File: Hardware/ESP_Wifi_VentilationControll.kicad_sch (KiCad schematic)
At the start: 38 parts, among them J1 programming, Q1 2N3904, Q2 2N3904, SW1 RST, SW2 BOOT, U1 LM1117-3.3, U2 ESP-12E, U3 ILD207T_D207, U4 ILD207T_D207, U5 XD-45_MH_MINI

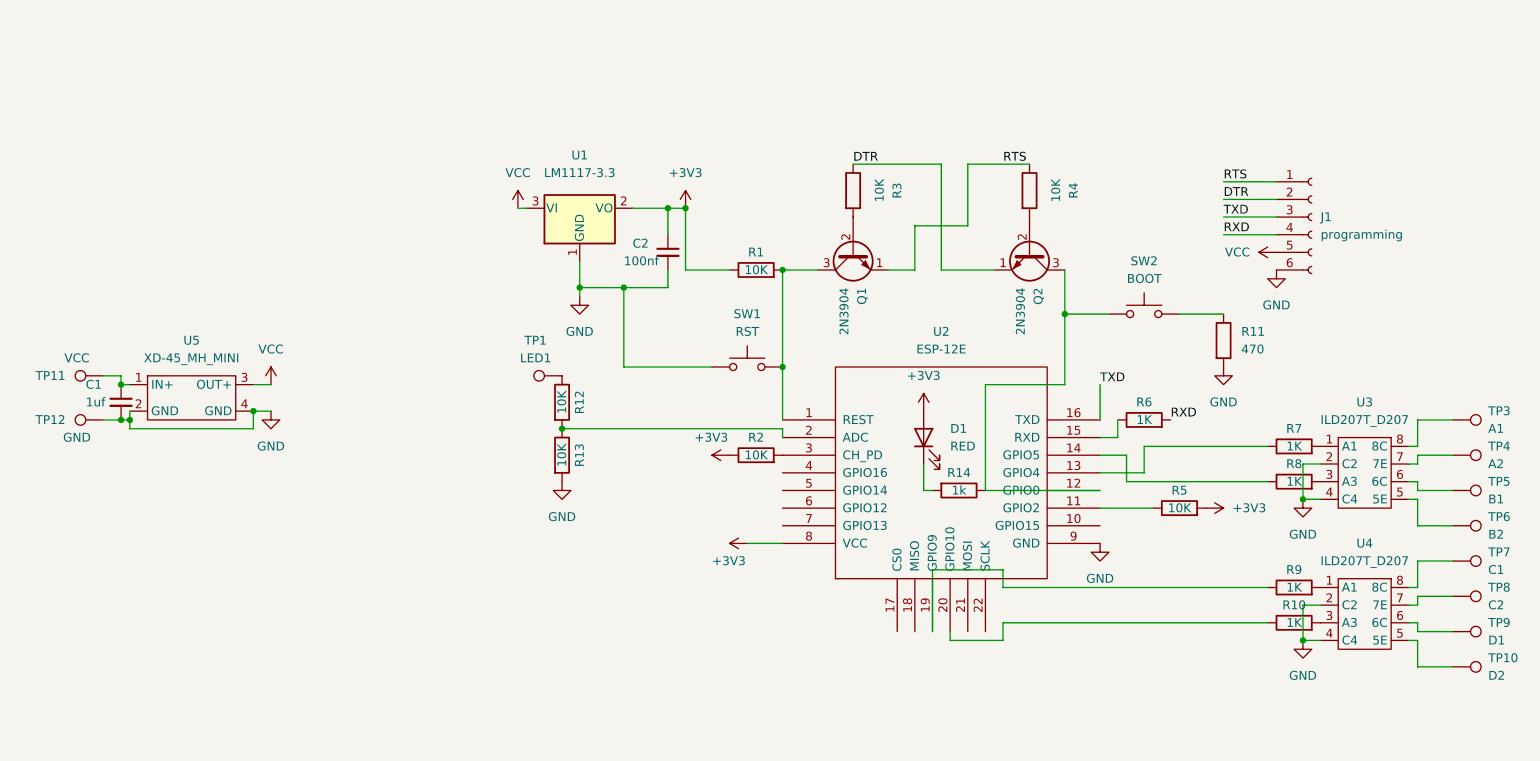
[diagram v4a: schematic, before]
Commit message: fixed some footprints and added missing resistor
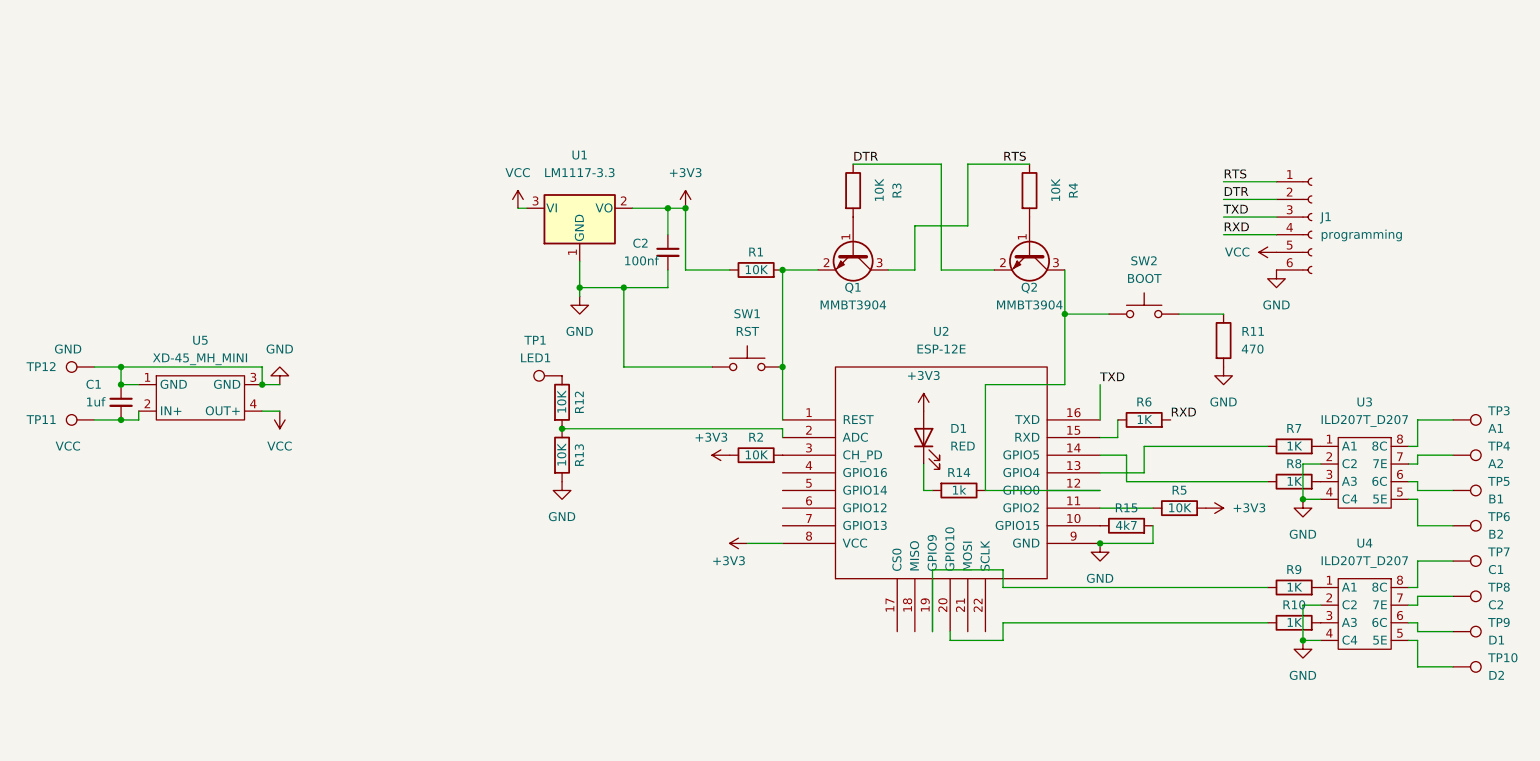
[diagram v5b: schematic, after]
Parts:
- removed Q1, Q2: 2N3904, Package_TO_SOT_SMD:SOT-23, symbol Transistor_BJT:2N3904
- added Q1, Q2: MMBT3904, Package_TO_SOT_SMD:SOT-23, symbol Transistor_BJT:MMBT3904
- added R15: 4k7, Resistor_SMD:R_1206_3216Metric, symbol Device:R
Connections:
- net DTR: now also Q2.2 (E)
- net GND: now also C1.1, U5.1 (GND), U5.3 (GND), R15.2; no longer C1.2, U5.2 (GND), U5.4 (GND)
- net RTS: now also Q1.3 (C)
- net VCC: now also U5.4 (OUT+); no longer U5.3 (OUT+)
- net at R1.2, SW1.2, U2.1 (REST): now also Q1.2 (E)
- net at U2.10 (GPIO15): now also R15.1
- net at R14.1, SW2.1, U2.12 (GPIO0): now also Q2.3 (C)
- net at R3.2: now also Q1.1 (B)
- net at R4.2: now also Q2.1 (B)
- new net: C1.2, TP11.1, U5.2 (IN+)
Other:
- moved on the sheet: TP11, TP12

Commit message: e
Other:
- moved on the sheet: C1, C2, D1, J1, Q1, Q2, R1, R10, R11, R12, R13, R14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
